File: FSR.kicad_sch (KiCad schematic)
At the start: 3 parts

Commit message: update: footprint link to component
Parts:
- C5: footprint G-Love:Capacitor_0603 -> MyGlove:Capacitor_0603
- FSR_1: footprint G-Love:PinHeader_1x02_Pas2.54mm_ -> MyGlove:PinHeader_1x02_Pas2.54mm_
- R1: footprint G-Love:Resistor_0603 -> MyGlove:Resistor_0603
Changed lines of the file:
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@@
 			)
 		)
-		(property "Footprint" "G-Love:Capacitor_0603"
+		(property "Footprint" "MyGlove:Capacitor_0603"
 			(at 30.48 48.26 0)
 			(hide yes)
@@
 			)
 		)
-		(property "Footprint" "G-Love:Resistor_0603"
+		(property "Footprint" "MyGlove:Resistor_0603"
 			(at 24.13 48.26 0)
 			(hide yes)
@@
 			)
 		)
-		(property "Footprint" "G-Love:PinHeader_1x02_Pas2.54mm_"
+		(property "Footprint" "MyGlove:PinHeader_1x02_Pas2.54mm_"
 			(at 24.13 30.48 0)
 			(hide yes)

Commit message: update ERC
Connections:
- net +5V renamed VCC
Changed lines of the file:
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@@
 	)
 	(symbol
-		(lib_id "G-Love:+5V")
+		(lib_id "G-Love:VCC")
 		(at 24.13 22.86 0)
 		(unit 1)
@@
 			)
 		)
-		(property "Value" "+5V"
+		(property "Value" "VCC"
 			(at 24.13 19.05 0)
 			(show_name no)

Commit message: Premier jet PCB, A optimiser
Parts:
- renumbered C5 to C13, R1 to R8
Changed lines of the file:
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@@
 		(in_pos_files yes)
 		(dnp no)
-		(property "Reference" "C5"
+		(property "Reference" "C13"
 			(at 32.004 47.244 0)
 			(show_name no)
@@
 			(project "G-Love"
 				(path "/808bc5ea-49ac-4454-ba77-8b20d01ce159/c9027db4-6968-4e40-a138-b60eacbff4db/15052d3f-5b94-4226-97e2-3e9ab10fafda"
-					(reference "C5")
+					(reference "C13")
 					(unit 1)
 				)
 				(path "/808bc5ea-49ac-4454-ba77-8b20d01ce159/c9027db4-6968-4e40-a138-b60eacbff4db/32c3dc22-6eac-49d0-b512-767615f82205"
-					(reference "C6")
+					(reference "C14")
 					(unit 1)
 				)
 				(path "/808bc5ea-49ac-4454-ba77-8b20d01ce159/c9027db4-6968-4e40-a138-b60eacbff4db/3f48e459-1dc8-4eb9-8adc-befbe01eab22"
-					(reference "C8")
+					(reference "C16")
 					(unit 1)
 				)
 				(path "/808bc5ea-49ac-4454-ba77-8b20d01ce159/c9027db4-6968-4e40-a138-b60eacbff4db/5442b494-eff8-4ddd-bc03-bcc1bea75842"
-					(reference "C7")
+					(reference "C15")
 					(unit 1)
 				)
 				(path "/808bc5ea-49ac-4454-ba77-8b20d01ce159/c9027db4-6968-4e40-a138-b60eacbff4db/f906f610-f118-4325-955e-6566f843376d"
-					(reference "C9")
+					(reference "C17")
 					(unit 1)
 				)
@@
 		(in_pos_files yes)
 		(dnp no)
-		(property "Reference" "R1"
+		(property "Reference" "R8"
 			(at 22.86 48.006 90)
 			(show_name no)
@@
 			(project "G-Love"
 				(path "/808bc5ea-49ac-4454-ba77-8b20d01ce159/c9027db4-6968-4e40-a138-b60eacbff4db/15052d3f-5b94-4226-97e2-3e9ab10fafda"
-					(reference "R1")
+					(reference "R8")
 					(unit 1)
 				)
 				(path "/808bc5ea-49ac-4454-ba77-8b20d01ce159/c9027db4-6968-4e40-a138-b60eacbff4db/32c3dc22-6eac-49d0-b512-767615f82205"
-					(reference "R2")
+					(reference "R9")
 					(unit 1)
 				)
 				(path "/808bc5ea-49ac-4454-ba77-8b20d01ce159/c9027db4-6968-4e40-a138-b60eacbff4db/3f48e459-1dc8-4eb9-8adc-befbe01eab22"
-					(reference "R4")
+					(reference "R11")
 					(unit 1)
 				)
 				(path "/808bc5ea-49ac-4454-ba77-8b20d01ce159/c9027db4-6968-4e40-a138-b60eacbff4db/5442b494-eff8-4ddd-bc03-bcc1bea75842"
-					(reference "R3")
+					(reference "R10")
 					(unit 1)
 				)
 				(path "/808bc5ea-49ac-4454-ba77-8b20d01ce159/c9027db4-6968-4e40-a138-b60eacbff4db/f906f610-f118-4325-955e-6566f843376d"
-					(reference "R5")
+					(reference "R12")
 					(unit 1)
 				)
@@
 		(dnp no)
 		(fields_autoplaced yes)
-		(property "Reference" "#PWR4"
+		(property "Reference" "#PWR09"
 			(at 27.94 24.638 0)
 			(hide yes)
@@
 			(project "G-Love"
 				(path "/808bc5ea-49ac-4454-ba77-8b20d01ce159/c9027db4-6968-4e40-a138-b60eacbff4db/15052d3f-5b94-4226-97e2-3e9ab10fafda"
-					(reference "#PWR4")
+					(reference "#PWR09")
 					(unit 1)
 				)
 				(path "/808bc5ea-49ac-4454-ba77-8b20d01ce159/c9027db4-6968-4e40-a138-b60eacbff4db/32c3dc22-6eac-49d0-b512-767615f82205"
-					(reference "#PWR5")
+					(reference "#PWR010")
 					(unit 1)
 				)
 				(path "/808bc5ea-49ac-4454-ba77-8b20d01ce159/c9027db4-6968-4e40-a138-b60eacbff4db/3f48e459-1dc8-4eb9-8adc-befbe01eab22"
-					(reference "#PWR7")
+					(reference "#PWR012")
 					(unit 1)
 				)
 				(path "/808bc5ea-49ac-4454-ba77-8b20d01ce159/c9027db4-6968-4e40-a138-b60eacbff4db/5442b494-eff8-4ddd-bc03-bcc1bea75842"
-					(reference "#PWR6")
+					(reference "#PWR011")
 					(unit 1)
 				)
 				(path "/808bc5ea-49ac-4454-ba77-8b20d01ce159/c9027db4-6968-4e40-a138-b60eacbff4db/f906f610-f118-4325-955e-6566f843376d"
-					(reference "#PWR8")
+					(reference "#PWR013")
 					(unit 1)
 				)
@@
 		(dnp no)
 		(fields_autoplaced yes)
-		(property "Reference" "GND09"
+		(property "Reference" "GND011"
 			(at 24.13 61.976 0)
 			(hide yes)
@@
 			(project "G-Love"
 				(path "/808bc5ea-49ac-4454-ba77-8b20d01ce159/c9027db4-6968-4e40-a138-b60eacbff4db/15052d3f-5b94-4226-97e2-3e9ab10fafda"
-					(reference "GND09")
+					(reference "GND011")
 					(unit 1)
 				)
 				(path "/808bc5ea-49ac-4454-ba77-8b20d01ce159/c9027db4-6968-4e40-a138-b60eacbff4db/32c3dc22-6eac-49d0-b512-767615f82205"
-					(reference "GND010")
+					(reference "GND012")
 					(unit 1)
 				)
 				(path "/808bc5ea-49ac-4454-ba77-8b20d01ce159/c9027db4-6968-4e40-a138-b60eacbff4db/3f48e459-1dc8-4eb9-8adc-befbe01eab22"
-					(reference "GND012")
+					(reference "GND014")
 					(unit 1)
 				)
 				(path "/808bc5ea-49ac-4454-ba77-8b20d01ce159/c9027db4-6968-4e40-a138-b60eacbff4db/5442b494-eff8-4ddd-bc03-bcc1bea75842"
-					(reference "GND011")
+					(reference "GND013")
 					(unit 1)
 				)
 				(path "/808bc5ea-49ac-4454-ba77-8b20d01ce159/c9027db4-6968-4e40-a138-b60eacbff4db/f906f610-f118-4325-955e-6566f843376d"
-					(reference "GND013")
-					(unit 1)
-				)
+					(reference "GND015")
+					(unit 1)
+				)

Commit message: reste routage mais peu
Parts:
- FSR_1: footprint MyGlove:PinHeader_1x02_Pas2.54mm_ -> MyGlove:PinHeader_1x02_P2.54mm_Vertical
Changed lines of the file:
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@@
 			)
 		)
-		(property "Footprint" "MyGlove:PinHeader_1x02_Pas2.54mm_"
+		(property "Footprint" "MyGlove:PinHeader_1x02_P2.54mm_Vertical"
 			(at 24.13 30.48 0)
 			(hide yes)

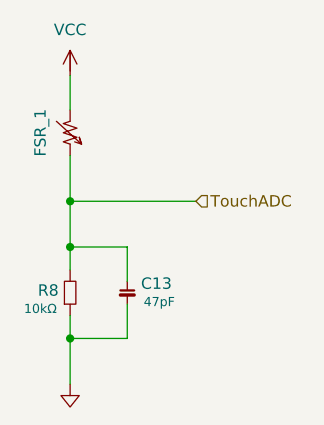
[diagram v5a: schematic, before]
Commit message: Silkscreen embetant
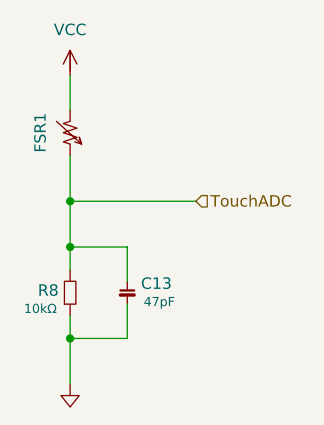
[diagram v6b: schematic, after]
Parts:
- renumbered FSR_1 to FSR1
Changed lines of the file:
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@@
 		(in_pos_files yes)
 		(dnp no)
-		(property "Reference" "FSR_1"
+		(property "Reference" "FSR1"
 			(at 20.828 30.48 0)
 			(show_name no)
@@
 			(project "G-Love"
 				(path "/808bc5ea-49ac-4454-ba77-8b20d01ce159/c9027db4-6968-4e40-a138-b60eacbff4db/15052d3f-5b94-4226-97e2-3e9ab10fafda"
-					(reference "FSR_1")
+					(reference "FSR1")
 					(unit 1)
 				)
 				(path "/808bc5ea-49ac-4454-ba77-8b20d01ce159/c9027db4-6968-4e40-a138-b60eacbff4db/32c3dc22-6eac-49d0-b512-767615f82205"
-					(reference "FSR_2")
+					(reference "FSR2")
 					(unit 1)
 				)
 				(path "/808bc5ea-49ac-4454-ba77-8b20d01ce159/c9027db4-6968-4e40-a138-b60eacbff4db/3f48e459-1dc8-4eb9-8adc-befbe01eab22"
-					(reference "FSR_4")
+					(reference "FSR4")
 					(unit 1)
 				)
 				(path "/808bc5ea-49ac-4454-ba77-8b20d01ce159/c9027db4-6968-4e40-a138-b60eacbff4db/5442b494-eff8-4ddd-bc03-bcc1bea75842"
-					(reference "FSR_3")
+					(reference "FSR3")
 					(unit 1)
 				)
 				(path "/808bc5ea-49ac-4454-ba77-8b20d01ce159/c9027db4-6968-4e40-a138-b60eacbff4db/f906f610-f118-4325-955e-6566f843376d"
-					(reference "FSR_5")
+					(reference "FSR5")
 					(unit 1)
 				)

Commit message: Passe ERC
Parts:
- renumbered C13 to C14
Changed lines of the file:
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@@
 		(in_pos_files yes)
 		(dnp no)
-		(property "Reference" "C13"
+		(property "Reference" "C14"
 			(at 32.004 47.244 0)
 			(show_name no)
@@
 			(project "G-Love"
 				(path "/808bc5ea-49ac-4454-ba77-8b20d01ce159/c9027db4-6968-4e40-a138-b60eacbff4db/15052d3f-5b94-4226-97e2-3e9ab10fafda"
-					(reference "C13")
+					(reference "C14")
 					(unit 1)
 				)
 				(path "/808bc5ea-49ac-4454-ba77-8b20d01ce159/c9027db4-6968-4e40-a138-b60eacbff4db/32c3dc22-6eac-49d0-b512-767615f82205"
-					(reference "C14")
+					(reference "C15")
 					(unit 1)
 				)
 				(path "/808bc5ea-49ac-4454-ba77-8b20d01ce159/c9027db4-6968-4e40-a138-b60eacbff4db/3f48e459-1dc8-4eb9-8adc-befbe01eab22"
+					(reference "C17")
+					(unit 1)
+				)
+				(path "/808bc5ea-49ac-4454-ba77-8b20d01ce159/c9027db4-6968-4e40-a138-b60eacbff4db/5442b494-eff8-4ddd-bc03-bcc1bea75842"
 					(reference "C16")
 					(unit 1)
 				)
-				(path "/808bc5ea-49ac-4454-ba77-8b20d01ce159/c9027db4-6968-4e40-a138-b60eacbff4db/5442b494-eff8-4ddd-bc03-bcc1bea75842"
-					(reference "C15")
-					(unit 1)
-				)
 				(path "/808bc5ea-49ac-4454-ba77-8b20d01ce159/c9027db4-6968-4e40-a138-b60eacbff4db/f906f610-f118-4325-955e-6566f843376d"
-					(reference "C17")
+					(reference "C18")
 					(unit 1)
 				)
@@
 		(dnp no)
 		(fields_autoplaced yes)
-		(property "Reference" "GND011"
+		(property "Reference" "GND012"
 			(at 24.13 61.976 0)
 			(hide yes)
@@
 			(project "G-Love"
 				(path "/808bc5ea-49ac-4454-ba77-8b20d01ce159/c9027db4-6968-4e40-a138-b60eacbff4db/15052d3f-5b94-4226-97e2-3e9ab10fafda"
-					(reference "GND011")
+					(reference "GND012")
 					(unit 1)
 				)
 				(path "/808bc5ea-49ac-4454-ba77-8b20d01ce159/c9027db4-6968-4e40-a138-b60eacbff4db/32c3dc22-6eac-49d0-b512-767615f82205"
-					(reference "GND012")
+					(reference "GND013")
 					(unit 1)
 				)
 				(path "/808bc5ea-49ac-4454-ba77-8b20d01ce159/c9027db4-6968-4e40-a138-b60eacbff4db/3f48e459-1dc8-4eb9-8adc-befbe01eab22"
+					(reference "GND015")
+					(unit 1)
+				)
+				(path "/808bc5ea-49ac-4454-ba77-8b20d01ce159/c9027db4-6968-4e40-a138-b60eacbff4db/5442b494-eff8-4ddd-bc03-bcc1bea75842"
 					(reference "GND014")
 					(unit 1)
 				)
-				(path "/808bc5ea-49ac-4454-ba77-8b20d01ce159/c9027db4-6968-4e40-a138-b60eacbff4db/5442b494-eff8-4ddd-bc03-bcc1bea75842"
-					(reference "GND013")
-					(unit 1)
-				)
 				(path "/808bc5ea-49ac-4454-ba77-8b20d01ce159/c9027db4-6968-4e40-a138-b60eacbff4db/f906f610-f118-4325-955e-6566f843376d"
-					(reference "GND015")
-					(unit 1)
-				)
+					(reference "GND016")
+					(unit 1)
+				)
